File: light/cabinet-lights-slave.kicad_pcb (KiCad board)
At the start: 2 copper layers, 50 x 50 mm, 15 parts, among them J1 NORTH, J2 EAST, J3 SOUTH, J4 WEST, Q1 NX7002AK, Q2 NTR1P02T1G

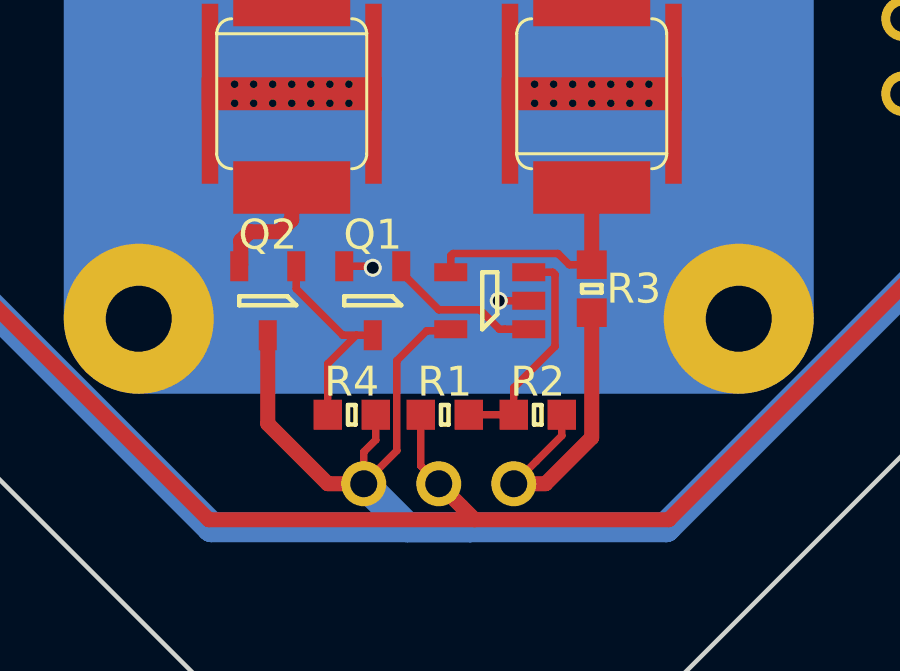
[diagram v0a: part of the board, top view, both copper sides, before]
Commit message: Tweak to use BJT transistor
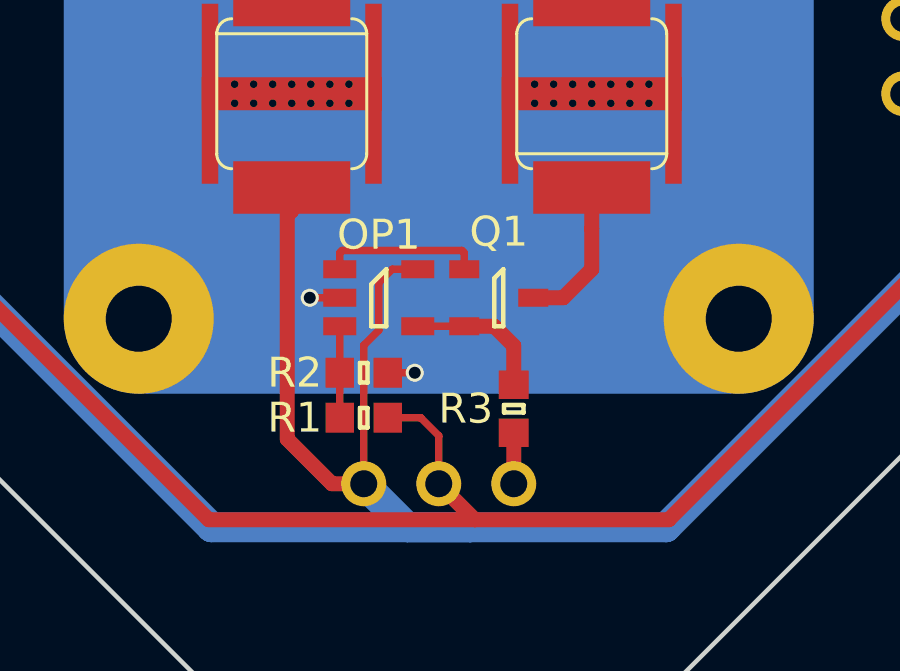
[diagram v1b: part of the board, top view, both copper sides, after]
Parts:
- removed Q2: NTR1P02T1G, agg:SOT-23
- removed R4: 1k, agg:0603
- Q1: value NX7002AK -> BC817-40
- moved R2 5.97 mm to (52.5, 66.8)
- moved R3 4.77 mm to (57.5, 68.0)
- moved Q1 4.20 mm to (57.0, 64.3), turned to 0 degrees
- moved OP1 3.70 mm to (53.0, 64.3), turned to 0 degrees
- moved R1 2.70 mm to (52.5, 68.3), turned to 0 degrees
- renumbered OP?1 to OP1
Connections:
- D1 pad 2: Net-(D1-Pad2) -> +12V
- D3 pad 1: /SENSE -> Net-(D3-Pad1)
- Q1 pad 2: GND -> /SENSE
- Q1 pad 3: Net-(Q1-Pad3) -> Net-(D3-Pad1)
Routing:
- net GND: track 12.6 -> 3.90 mm
- net Net-(Q1-Pad3): track 6.99 -> 0.00 mm
- net Net-(D3-Pad1): track 0.00 -> 5.48 mm
- net /DIM/100: track 7.65 -> 3.05 mm
- net Net-(D1-Pad2): track 3.94 -> 0.00 mm
- net +12V: track 146.5 -> 150.2 mm
- net /SENSE: track 8.43 -> 4.77 mm
- net /DIM: track 122.5 -> 123.5 mm

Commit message: Mounting holes, some track shenanigans
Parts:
- added X1: MOUNT, Mounting_Holes:MountingHole_2.7mm_M2.5, F.Cu at (37.5, 72.5)
- added X2: MOUNT, Mounting_Holes:MountingHole_2.7mm_M2.5, F.Cu at (37.5, 37.5)
- added X3: MOUNT, Mounting_Holes:MountingHole_2.7mm_M2.5, F.Cu at (72.5, 72.5)
- added X4: MOUNT, Mounting_Holes:MountingHole_2.7mm_M2.5, F.Cu at (72.5, 37.5)
- moved R1 1.79 mm to (54.1, 69.0)
- moved R2 1.79 mm to (54.1, 67.5)
- moved D1 0.60 mm to (49.5, 57.5)
- moved Q1 0.47 mm to (56.5, 64.4), turned to 90 degrees
- moved D3 0.40 mm to (60.5, 57.5)
- moved OP1 0.30 mm to (53.0, 64.6), turned to 90 degrees
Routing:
- net +12V: track 150.2 -> 25.6 mm
- net /DIM: track 123.5 -> 118.8 mm
- net GND: track 3.90 -> 7.80 mm
- net /DIM/100: track 3.05 -> 3.65 mm
- net Net-(D1-Pad1): track 8.42 -> 8.96 mm
- added copper zone on B.Cu, net +12V
- added copper zone on F.Cu, net +12V
- added copper zone on F.Cu, net /SENSE
- added copper zone on F.Cu, net GND
- added copper zone on F.Cu, net Net-(D1-Pad1)
- added copper zone on F.Cu, net Net-(D2-Pad1)
- added copper zone on F.Cu, net Net-(D3-Pad1)
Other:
- outline, holes or cut-outs redrawn
